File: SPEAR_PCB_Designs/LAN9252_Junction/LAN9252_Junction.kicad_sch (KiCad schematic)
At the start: 2 parts

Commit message: Almost finished board
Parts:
- R1: renamed from R51; footprint Resistor_SMD:R_0603_1608Metric -> Resistor_SMD:R_0402_1005Metric
- R2: renamed from R52; footprint Resistor_SMD:R_0603_1608Metric -> Resistor_SMD:R_0402_1005Metric
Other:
- added sheet Buck Converter (C:/Users/sheeb/OneDrive/Documents/IGuessThisIsTheFinalBoard(s)/pcb_designs_2026/SPEAR_PCB_Designs/AP63203BuckConverter/AP63203BuckConverter.kicad_sch)
- moved on the sheet: R1, R2

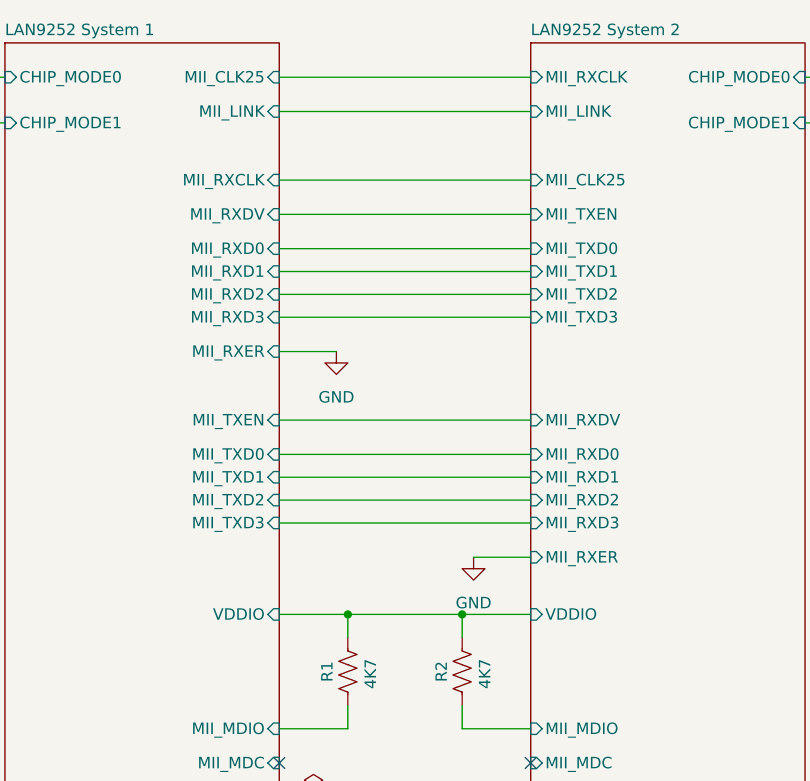
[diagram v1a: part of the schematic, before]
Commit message: Updated Junction board
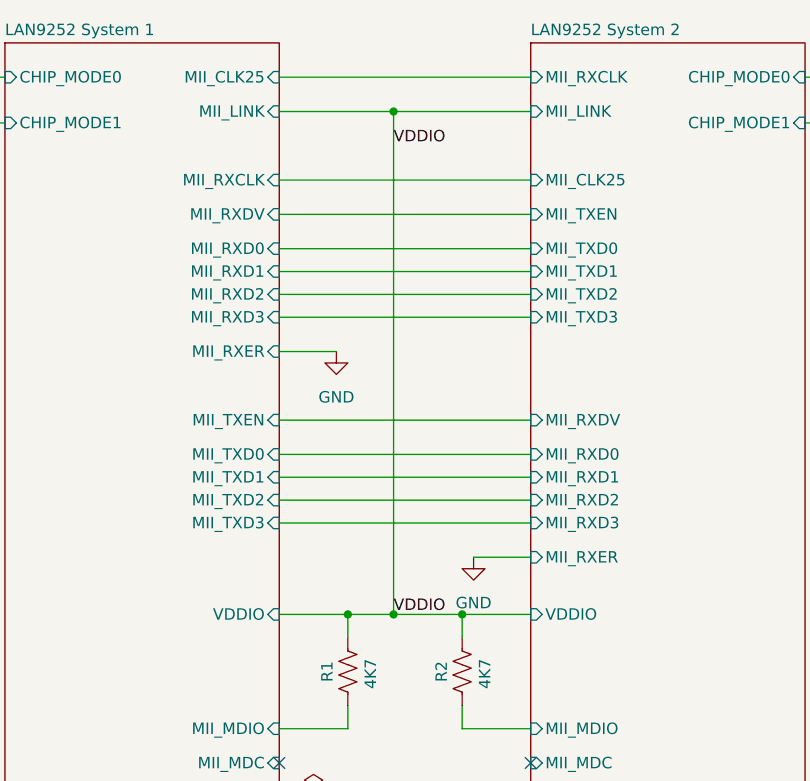
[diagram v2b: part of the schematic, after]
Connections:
- net LAN9252 System 1/VDDIO renamed VDDIO
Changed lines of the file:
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@@
+	)
+	(junction
+		(at 119.38 113.03)
+		(diameter 0)
+		(color 0 0 0 0)
 	)
 	(junction
@@
 	(junction
 		(at 127 113.03)
+		(diameter 0)
+		(color 0 0 0 0)
+	)
+	(junction
+		(at 119.38 57.15)
 		(diameter 0)
 		(color 0 0 0 0)
@@
 	(wire
 		(pts
+			(xy 119.38 57.15) (xy 119.38 113.03)
+		)
+		(stroke
+			(width 0)
+			(type default)
+		)
+	)
+	(wire
+		(pts
 			(xy 106.68 83.82) (xy 113.03 83.82)
 		)
@@
 	(wire
 		(pts
+			(xy 119.38 113.03) (xy 127 113.03)
+		)
+		(stroke
+			(width 0)
+			(type default)
+		)
+	)
+	(wire
+		(pts
 			(xy 106.68 64.77) (xy 134.62 64.77)
 		)
@@
 	(wire
 		(pts
-			(xy 114.3 113.03) (xy 127 113.03)
+			(xy 114.3 113.03) (xy 119.38 113.03)
 		)
 		(stroke
@@
 	(wire
 		(pts
-			(xy 106.68 57.15) (xy 134.62 57.15)
+			(xy 106.68 57.15) (xy 119.38 57.15)
 		)
 		(stroke
@@
 	(wire
 		(pts
+			(xy 119.38 57.15) (xy 134.62 57.15)
+		)
+		(stroke
+			(width 0)
+			(type default)
+		)
+	)
+	(wire
+		(pts
 			(xy 134.62 113.03) (xy 127 113.03)
 		)
@@
 		)
 	)
+	(label "VDDIO"
+		(at 119.38 60.96 0)
+		(effects
+			(font
+				(size 1.27 1.27)
+			)
+			(justify left bottom)
+		)
+	)
+	(label "VDDIO"
+		(at 119.38 113.03 0)
+		(effects
+			(font
+				(size 1.27 1.27)
+			)
+			(justify left bottom)
+		)
+	)

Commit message: Updated Junction Board
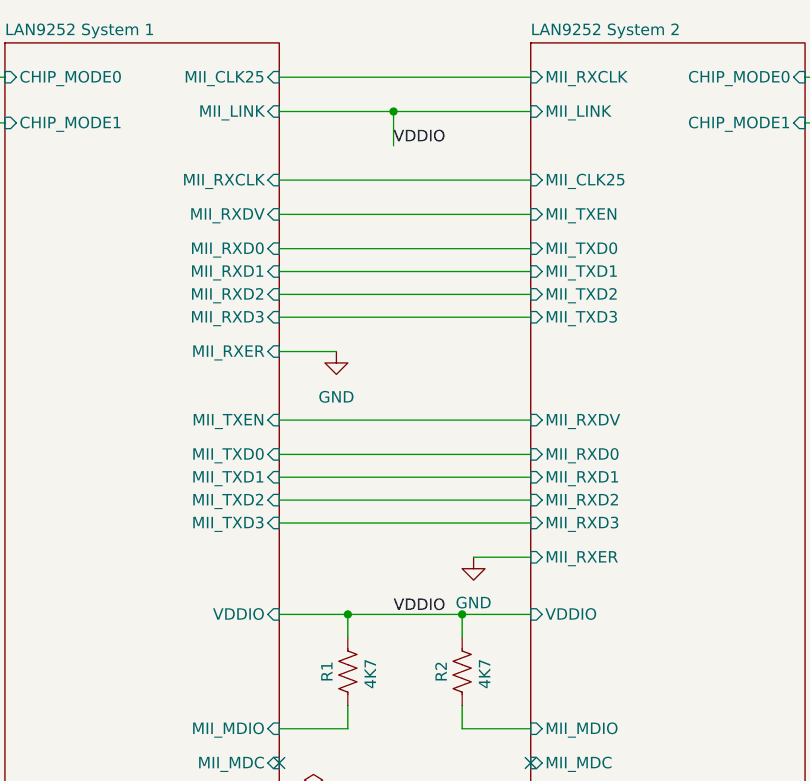
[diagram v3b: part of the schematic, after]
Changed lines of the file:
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@@
-	)
-	(junction
-		(at 119.38 113.03)
-		(diameter 0)
-		(color 0 0 0 0)
 	)
 	(junction
@@
 	(wire
 		(pts
+			(xy 119.38 57.15) (xy 134.62 57.15)
+		)
+		(stroke
+			(width 0)
+			(type default)
+		)
+	)
+	(wire
+		(pts
 			(xy 106.68 100.33) (xy 134.62 100.33)
 		)
@@
 	(wire
 		(pts
-			(xy 119.38 57.15) (xy 119.38 113.03)
-		)
-		(stroke
-			(width 0)
-			(type default)
-		)
-	)
-	(wire
-		(pts
 			(xy 106.68 83.82) (xy 113.03 83.82)
 		)
@@
 	(wire
 		(pts
-			(xy 119.38 113.03) (xy 127 113.03)
-		)
-		(stroke
-			(width 0)
-			(type default)
-		)
-	)
-	(wire
-		(pts
 			(xy 106.68 64.77) (xy 134.62 64.77)
 		)
@@
 	(wire
 		(pts
-			(xy 114.3 113.03) (xy 119.38 113.03)
+			(xy 114.3 113.03) (xy 127 113.03)
+		)
+		(stroke
+			(width 0)
+			(type default)
+		)
+	)
+	(wire
+		(pts
+			(xy 119.38 57.15) (xy 119.38 60.96)
 		)
 		(stroke
@@
 	(wire
 		(pts
+			(xy 106.68 102.87) (xy 134.62 102.87)
+		)
+		(stroke
+			(width 0)
+			(type default)
+		)
+	)
+	(wire
+		(pts
+			(xy 127 113.03) (xy 127 115.57)
+		)
+		(stroke
+			(width 0)
+			(type default)
+		)
+	)
+	(wire
+		(pts
 			(xy 106.68 57.15) (xy 119.38 57.15)
 		)
 		(stroke
-			(width 0)
-			(type default)
-		)
-	)
-	(wire
-		(pts
-			(xy 106.68 102.87) (xy 134.62 102.87)
-		)
-		(stroke
-			(width 0)
-			(type default)
-		)
-	)
-	(wire
-		(pts
-			(xy 127 113.03) (xy 127 115.57)
-		)
-		(stroke
-			(width 0)
-			(type default)
-		)
-	)
-	(wire
-		(pts
-			(xy 119.38 57.15) (xy 134.62 57.15)
-		)
-		(stroke

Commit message: Added BOM for the Junction Board
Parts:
- R1, R2: DigiKey_Part_Number (none) -> 311-4.7KJRCT-ND
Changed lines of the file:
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@@
+			)
+		)
+		(property "DigiKey_Part_Number" "311-4.7KJRCT-ND"
+			(at 127 119.38 90)
+			(effects
+				(font
+					(size 1.27 1.27)
+				)
+				(hide yes)
 			)
 		)
@@
 			(effects
 				(font
+					(size 1.27 1.27)
+				)
+				(hide yes)
+			)
+		)
+		(property "DigiKey_Part_Number" "311-4.7KJRCT-ND"
+			(at 114.3 119.38 90)
+			(effects
+				(font
